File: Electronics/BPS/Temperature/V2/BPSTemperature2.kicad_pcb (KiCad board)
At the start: 2 copper layers, 82 x 65 mm, 81 parts, among them J1 Conn_02x10_Counter_Clockwise, J2 Logic Analyzer, J3 Conn_02x06_Counter_Clockwise, J4 Conn_02x06_Counter_Clockwise, J5 Conn_01x02, SW1 SW_DIP_x06, U1 LTC2983

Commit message: Interim change
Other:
- board text added: "UTSVT - BPS Temperature v1.0 Spring 2019 Corbin Capo"
- board text removed: "Corbin Capo UTSVT Spring 2019 Temperature Board"
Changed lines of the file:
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@@
   (module "UTSVT_Connectors:43650-0202_01x02_Microfit 3.0_horizontal" (layer F.Cu)
     (at 118.1735 70.612 180)
-    (fp_text reference J5 (at 4.826 -10.8585 180) (layer F.SilkS)
+    (fp_text reference J5 (at 10.8585 -1.4605 180) (layer F.SilkS)
       (effects (font (size 1 1) (thickness 0.15)))
     )
@@
       (net 22 +5V))
   )
-  (gr_text "Corbin Capo\nUTSVT Spring 2019\nTemperature Board" (at 109.601 87.249) (layer F.SilkS)
+  (gr_text "UTSVT - BPS\nTemperature v1.0\nSpring 2019\nCorbin Capo" (at 108.458 87.1855) (layer F.SilkS)
     (effects (font (size 1.5 1.5) (thickness 0.3)))
   )
@@
     (connect_pads (clearance 0.508))
     (min_thickness 0.254)
-    (fill yes (arc_segments 16) (thermal_gap 0.508) (thermal_bridge_width 0.508))
+    (fill (arc_segments 16) (thermal_gap 0.508) (thermal_bridge_width 0.508))
     (polygon
       (pts
@@
     (connect_pads (clearance 0.508))
     (min_thickness 0.254)
-    (fill yes (arc_segments 16) (thermal_gap 0.508) (thermal_bridge_width 0.508))
+    (fill (arc_segments 16) (thermal_gap 0.508) (thermal_bridge_width 0.508))
     (polygon
       (pts

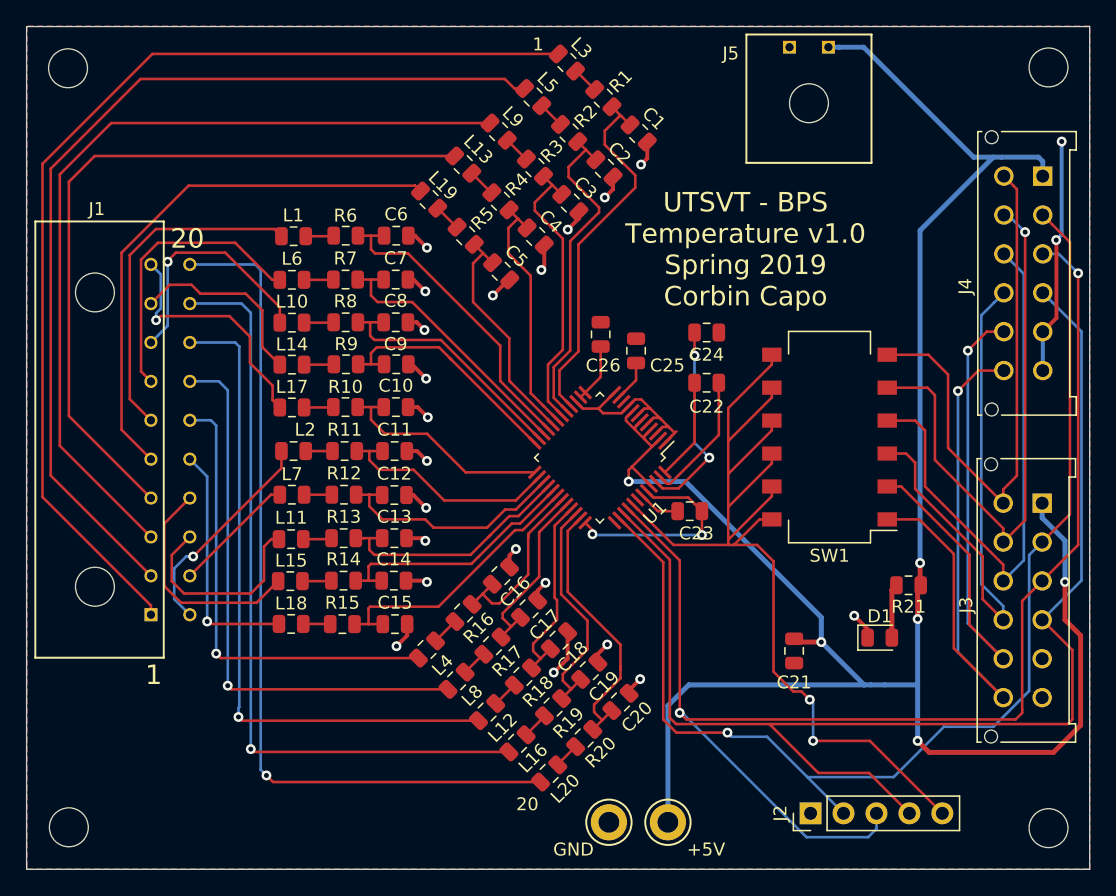
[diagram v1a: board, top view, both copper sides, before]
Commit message: Added logos and references
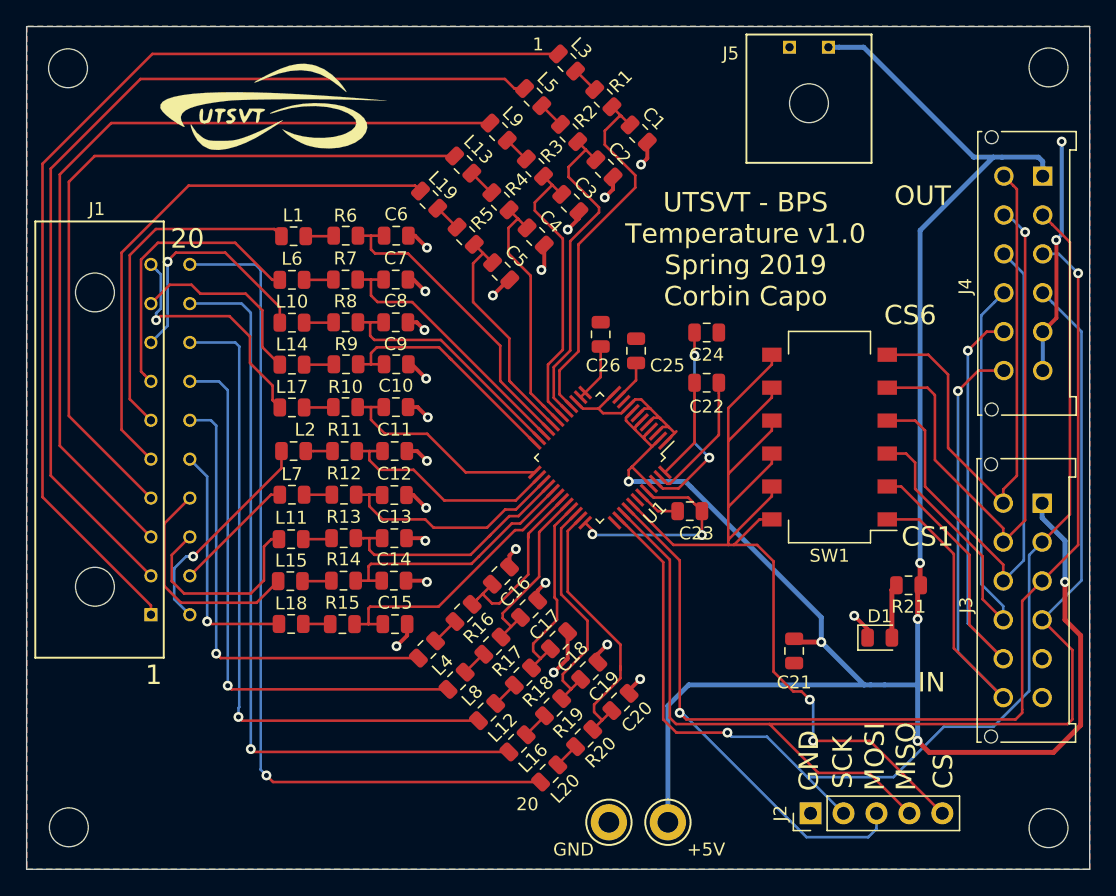
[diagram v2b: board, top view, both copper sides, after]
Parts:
- added G***: LOGO, UTSVT_Special:UTSVT_Logo_Symbol, F.Cu at (71.8, 76.3)
- added G***: LOGO, UTSVT_Special:Hallock_Image, B.Cu at (85.9, 108.7)
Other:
- board text added: "CS"
- board text added: "CS1"
- board text added: "CS6"
- board text added: "GND"
- board text added: "IN"
- board text added: "MISO"
- board text added: "MOSI"
- board text added: "OUT"
- board text added: "SCK"
- board text added: "Spring 2019: Monolo Alvarez Chase Block Corbin Capo Richard Li Austin Tsao Garrett Wong Sihyung Woo Sijin Woo"
- board text removed: "Monolo Alvarez Chase Block Richard Li Garrett Wong Sijin Woo Temperature Board UTSVT-Spring 2019"

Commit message: Hopefully final reference edit
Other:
- board text added: "+5V"
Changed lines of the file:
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@@
   (general
     (thickness 1.6)
-    (drawings 19)
+    (drawings 21)
     (tracks 689)
     (zones 0)
@@
   (module "UTSVT_Connectors:43650-0202_01x02_Microfit 3.0_horizontal" (layer F.Cu)
     (at 118.1735 70.612 180)
-    (fp_text reference J5 (at 10.8585 -1.4605 180) (layer F.SilkS)
+    (fp_text reference J5 (at 10.795 -5.1435 180) (layer F.SilkS)
       (effects (font (size 1 1) (thickness 0.15)))
     )
@@
       (xy -3.770496 -5.687082) (xy -3.551303 -5.609675) (xy -3.473034 -5.588) (xy -3.408236 -5.646283)) (layer B.SilkS) (width 0.01))
   )
+  (gr_text +5V (at 120.9675 71.9455) (layer F.SilkS)
+    (effects (font (size 1.5 1.5) (thickness 0.3)))
+  )
+  (gr_text GND (at 106.1085 71.9455) (layer F.SilkS)
+    (effects (font (size 1.5 1.5) (thickness 0.3)))
+  )
   (gr_text CS1 (at 122.4915 109.347) (layer F.SilkS)

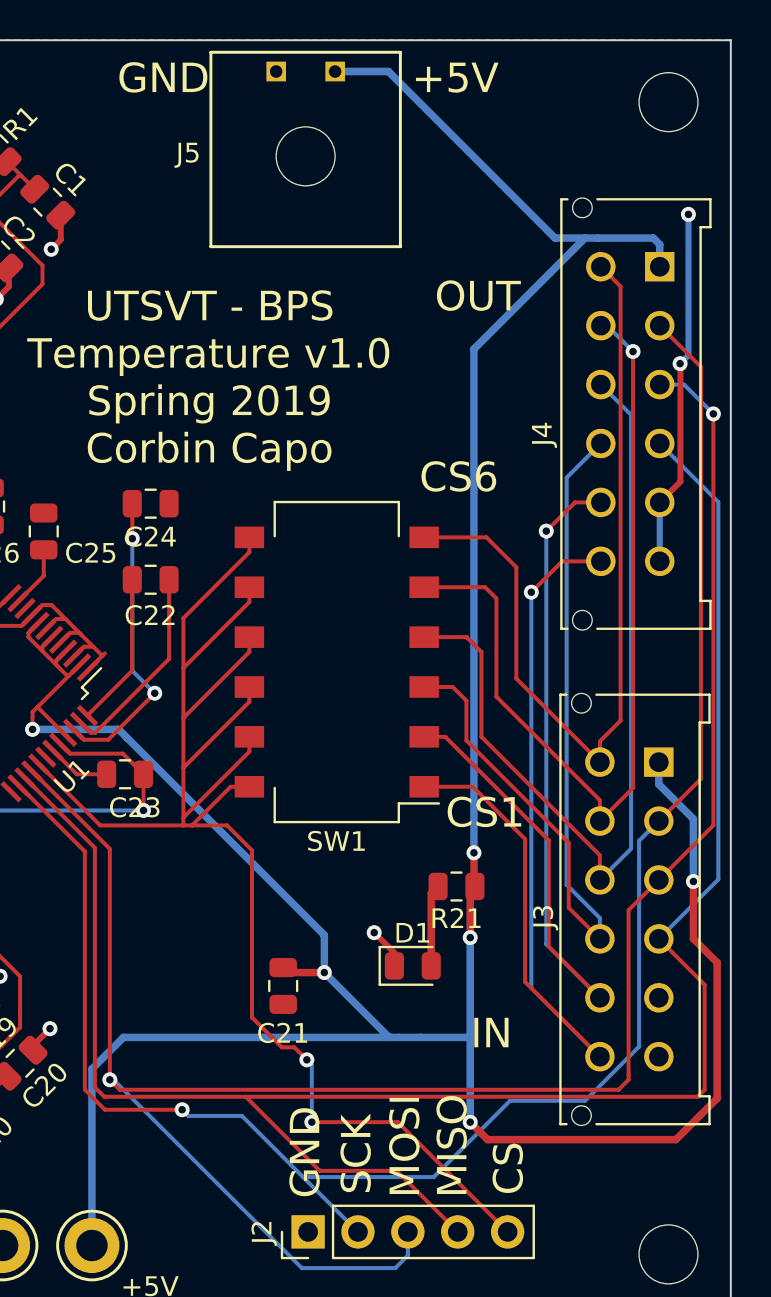
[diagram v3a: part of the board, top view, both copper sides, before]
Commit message: New connector for Temperature Board for BPS
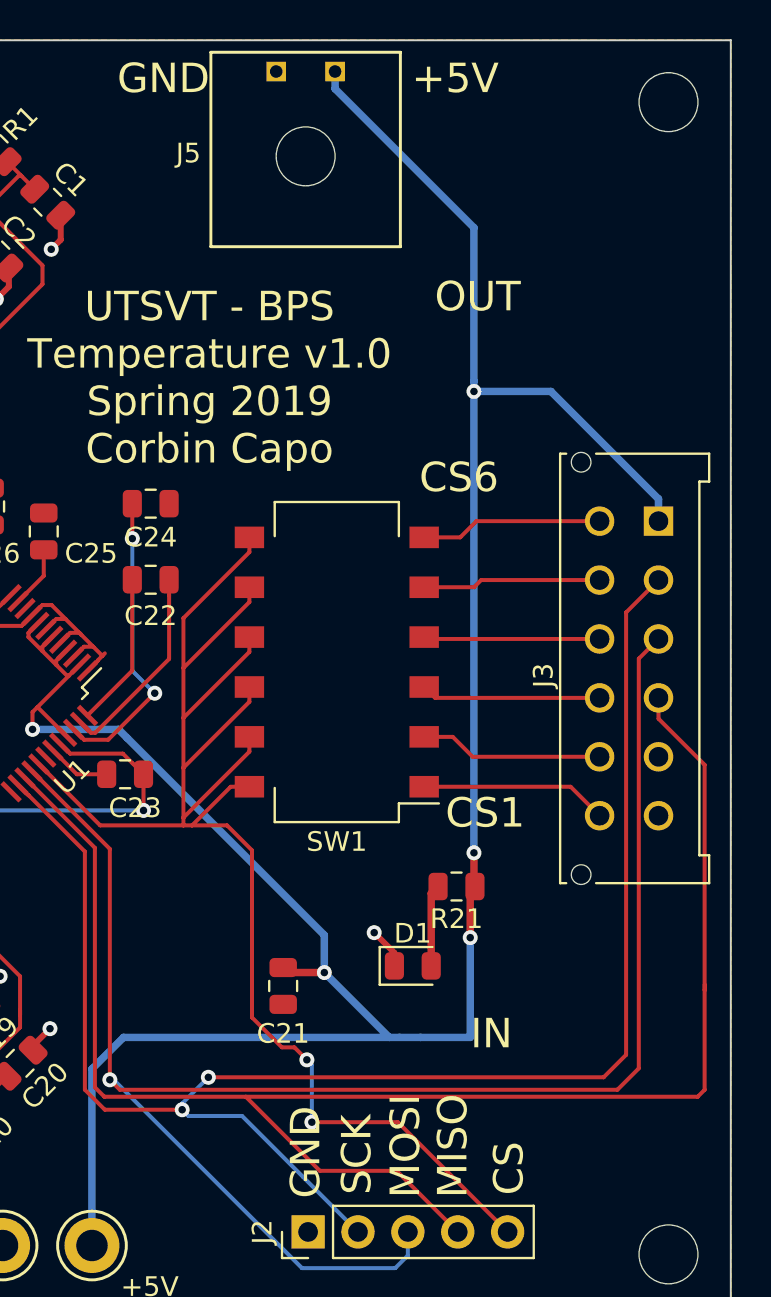
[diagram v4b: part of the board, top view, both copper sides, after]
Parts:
- removed J4: Conn_02x06_Counter_Clockwise, UTSVT_Connectors:Molex_MicroFit3.0_2x6xP3.00mm_PolarizingPeg_Vertical
- moved J3 12.3 mm to (131.3, 94.5)
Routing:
- net /CS1: track 48.2 -> 9.54 mm, vias 1 -> 0
- net /CS2: track 45.9 -> 9.35 mm, vias 1 -> 0
- net +5V: track 170.2 -> 134.3 mm, vias 6 -> 5
- net /CS5: track 44.2 -> 9.08 mm, vias 1 -> 0
- net /CS4: track 43.9 -> 8.97 mm
- net /CS3: track 44.0 -> 9.16 mm
- net /CS6: track 43.1 -> 9.27 mm
- net GND: track 90.1 -> 71.8 mm, vias 25 -> 23
- net /MOSI: track 103.9 -> 87.9 mm, vias 2 -> 1
- net /MISO: track 98.6 -> 83.5 mm
- net /SCK: track 92.6 -> 82.7 mm, vias 1 -> 2
